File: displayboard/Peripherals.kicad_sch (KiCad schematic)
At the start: 13 parts, among them IC1101 PCAL6416AHF, SW1101 Button 1, SW1102 Button 2, SW1103 Button 3, SW1104 Button 4

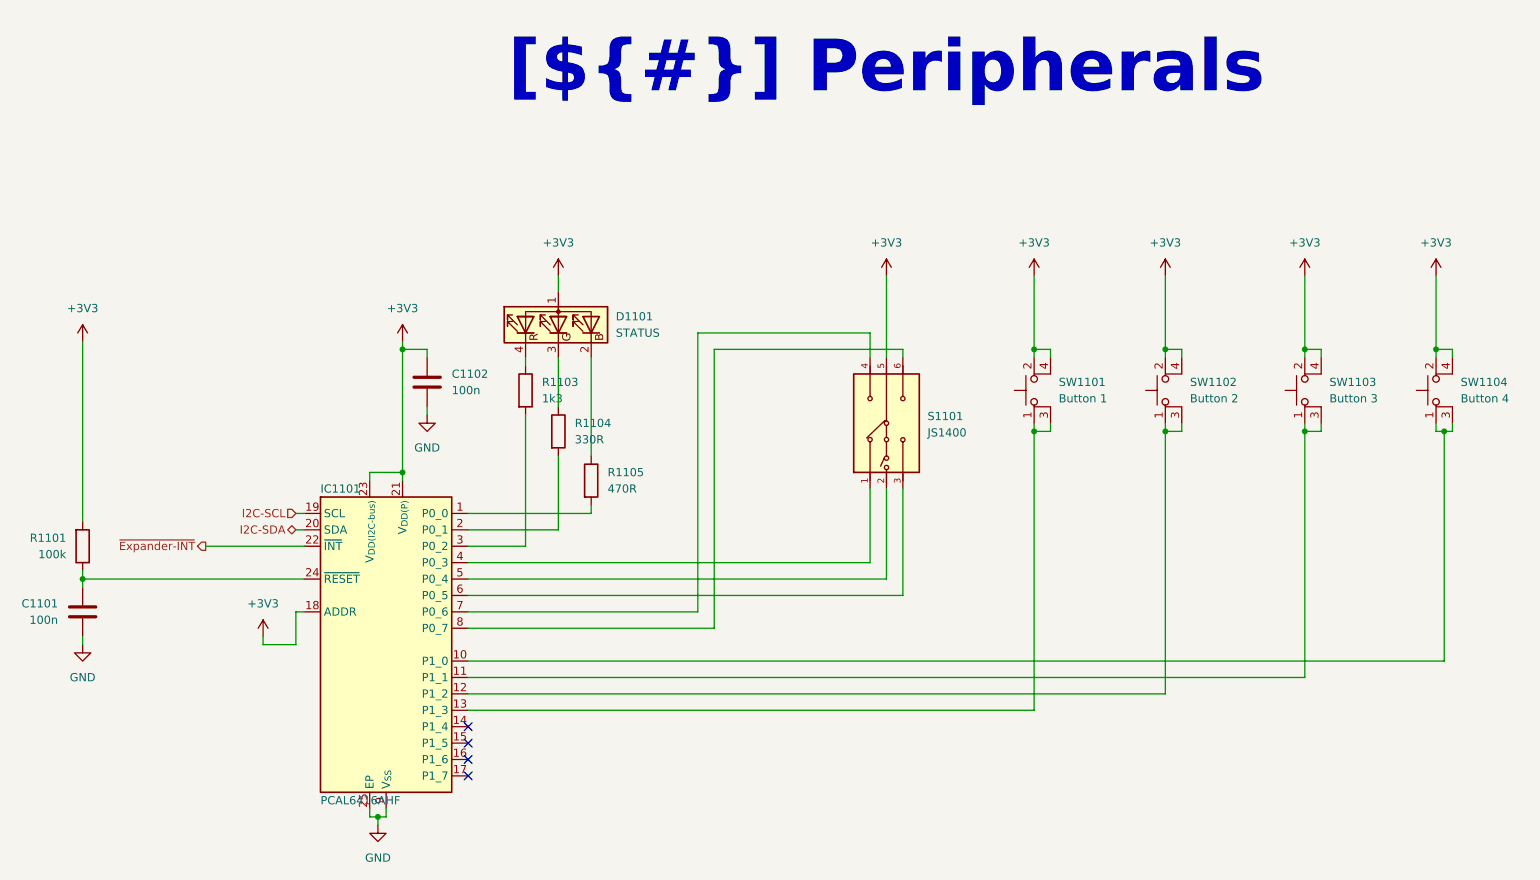
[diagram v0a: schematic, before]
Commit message: Remove old production files, add cutout for the programming cable, add connector for mainboard cable
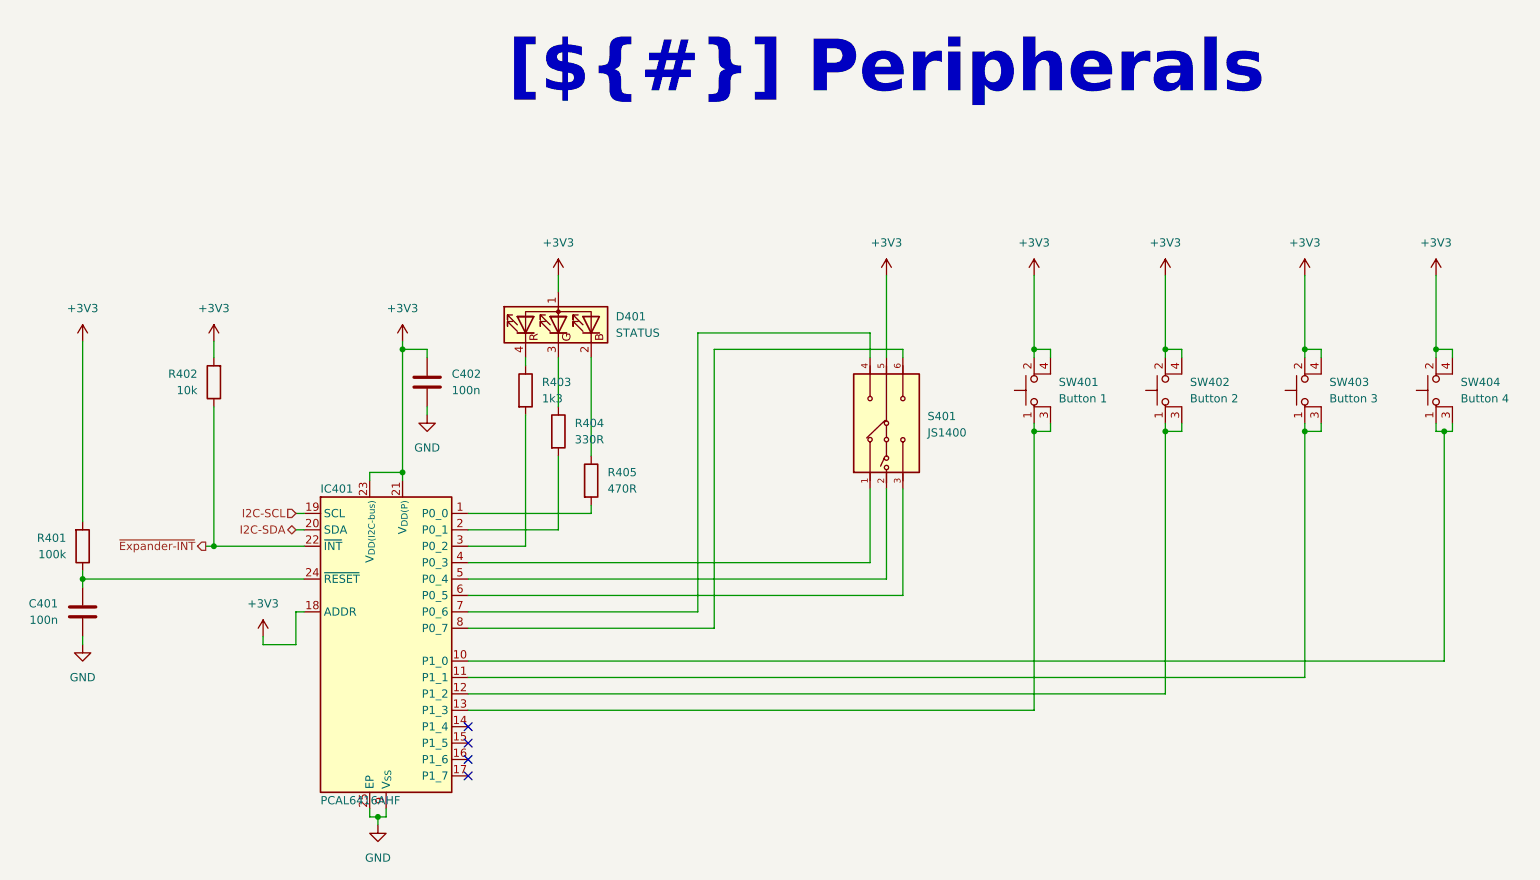
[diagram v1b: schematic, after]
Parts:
- added R402: 10k, Resistor_SMD:R_0805_2012Metric, symbol Device:R
- renumbered C1101 to C401, C1102 to C402, D1101 to D401, IC1101 to IC401, R1101 to R401, R1103 to R403, R1104 to R404, R1105 to R405, S1101 to S401, SW1101 to SW401, SW1102 to SW402, SW1103 to SW403, SW1104 to SW404
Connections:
- net +3V3: now also R402.2
- net ~{Expander-INT}: now also R402.1
